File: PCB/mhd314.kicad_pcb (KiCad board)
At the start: 4 copper layers, 65 x 56 mm, 193 parts, among them J1 Raspberry_Pi_2_3, J2 AudioJack_Pentaconn, J4 AudioJack3_SwitchTR, Q1 AO3401A, SW1 SW_Push, U1 ES9038Q2M, U10 AT24CS64-SSHM, U11 OPA1622, U13 OPA1622, U2 OPA1612AxD, U3 OPA1612AxD, U4 OPA1622, U5 LM317_SOT-223, U6 LM317_SOT-223, U7 TPS65131RGE, U8 LM317_SOT-223, U9 LM337_SOT223, Y1 ASE-50MHz

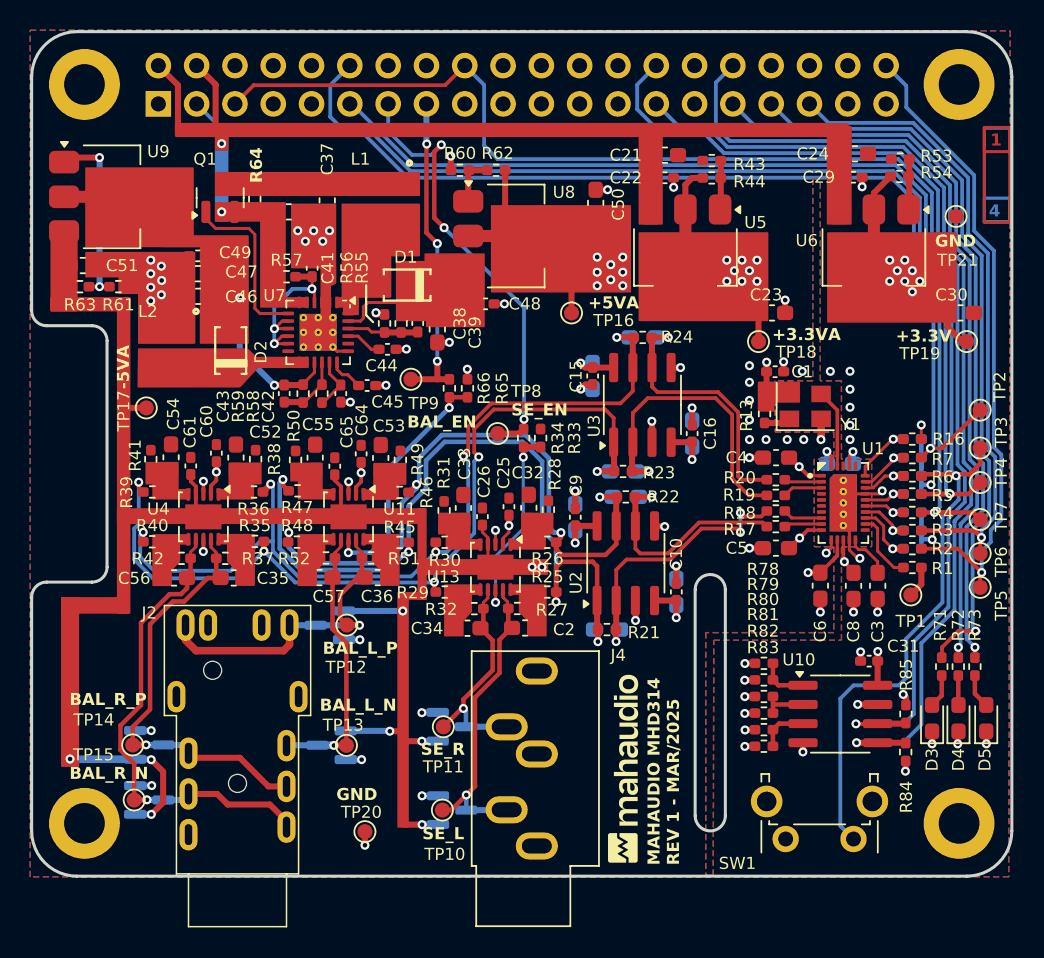
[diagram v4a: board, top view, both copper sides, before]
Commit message: Changed single ended connector for gold plated part and changed resistor and capacitor values of opa1622 amp for improved power on high impedance headphones
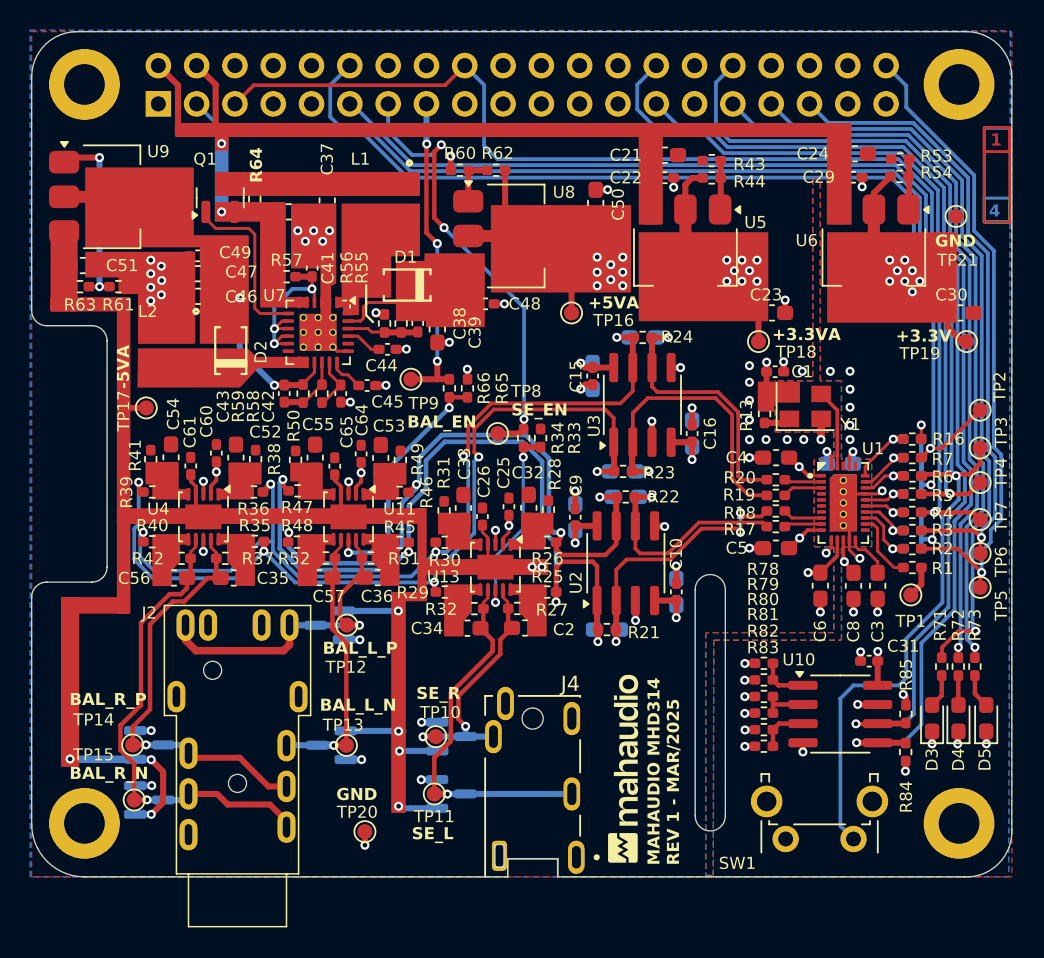
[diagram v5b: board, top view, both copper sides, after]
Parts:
- C13, C14, C19, C20: value 1.2nF -> 820pF
- C2, C32, C33, C34, C35, C36, C52, C53, C54, C55, C56, C57: value DNP -> 820pF
- J4: value AudioJack3_SwitchTR -> AudioJack4; footprint Connector_Audio:Jack_3.5mm_CUI_SJ1-3535NG_Horizontal -> mahaudio KiCad Library:TENSILITY_54-00176
- R27, R28, R31, R32: value 330R -> 442R
- R37, R38, R41, R42, R49, R50, R51, R52: value 174R -> 442R
- moved TP10 4.89 mm to (126.9, 90.7)
- moved D6 4.87 mm to (127.9, 90.7)
- moved TP11 4.49 mm to (126.8, 94.5)
- moved D7 4.46 mm to (127.9, 94.5)
- moved J4 3.96 mm to (133.3, 94.0), turned to 0 degrees
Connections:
- J4 pad TN: unconnected-(J4-PadTN) -> (no net)
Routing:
- net /OUT_SE_R: track 15.1 -> 24.8 mm
- net /OUT_SE_L: track 20.8 -> 17.2 mm, vias 1 -> 2
- net -5VA: track 40.1 -> 41.1 mm
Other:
- board size 65 x 56 mm -> 65 x 56.1 mm

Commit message: Changes in E2P for better identification of the board
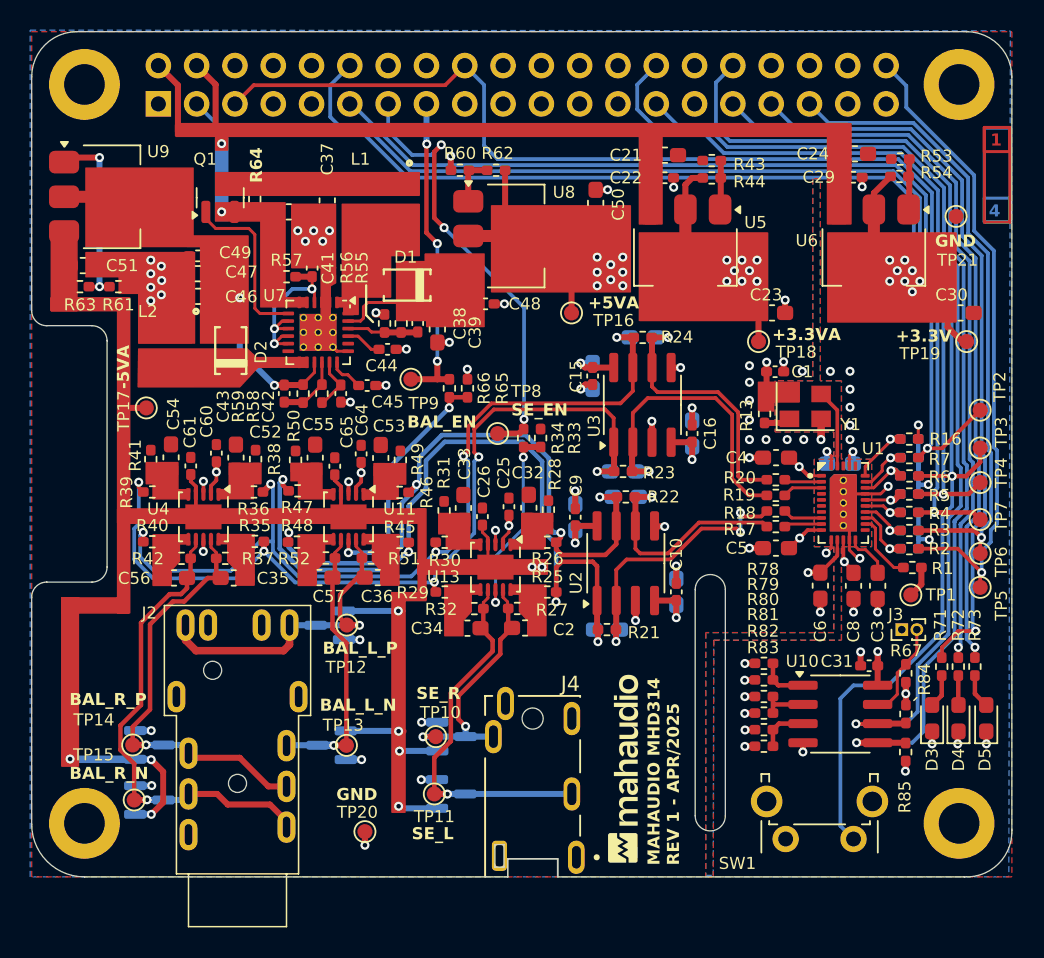
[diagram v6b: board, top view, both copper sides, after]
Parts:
- added J3: Conn_01x02_Pin, Connector_PinHeader_1.00mm:PinHeader_1x02_P1.00mm_Vertical, F.Cu at (157.8, 83.6)
- added R67: 1k, Resistor_SMD:R_0402_1005Metric_Pad0.72x0.64mm_HandSolder, F.Cu at (158.1, 86.5)
- R27, R28, R31, R32, R37, R38, R41, R42, R49, R50, R51, R52: value 442R -> 430R
- R8, R84, R85, R9: value 2k -> 3.9k
- moved C31 0.31 mm to (155.6, 86.0)
- moved R15 0.20 mm to (158.3, 71.0)
- moved R16 0.20 mm to (158.3, 71.0)
- moved R3 0.20 mm to (158.3, 77.0)
- moved R10 0.20 mm to (158.3, 78.2)
- moved R11 0.20 mm to (158.3, 77.0)
- moved R12 0.20 mm to (158.3, 75.8)
- moved R14 0.20 mm to (158.3, 74.6)
- moved R2 0.20 mm to (158.3, 78.2)
- moved R4 0.20 mm to (158.3, 75.8)
- moved R5 0.20 mm to (158.3, 74.6)
- moved R6 0.20 mm to (158.3, 73.4)
- moved R7 0.20 mm to (158.3, 72.2)
- moved R8 0.20 mm to (158.3, 73.4)
- moved R9 0.20 mm to (158.3, 72.2)
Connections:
- U10 pad 7: GND -> Net-(J3-Pin_2)
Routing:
- net Net-(J3-Pin_2): track 0.00 -> 6.31 mm
- net /DAC_RESETB: track 68.7 -> 65.5 mm
- net +3.3V: track 24.8 -> 26.3 mm
- net GND: track 54.2 -> 53.4 mm, vias 73 -> 72
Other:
- board text added: "MAHAUDIO MHD314 REV 1 - APR/2025"
- board text removed: "MAHAUDIO MHD314 REV 1 - MAR/2025"
